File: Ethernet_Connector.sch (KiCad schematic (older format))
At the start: 1 part, among them Con2 WE-RJ45_7498011122AR

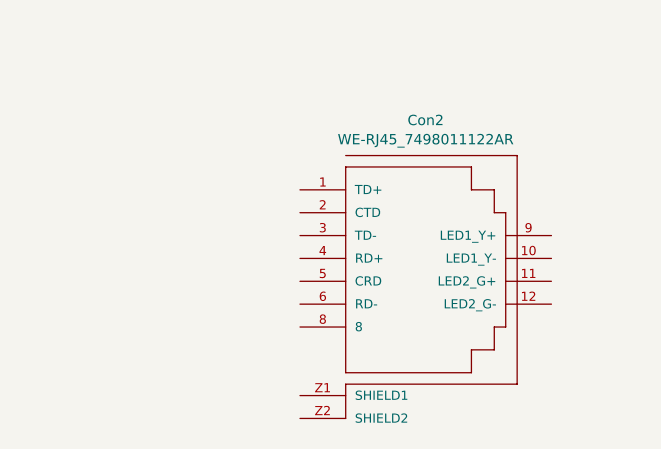
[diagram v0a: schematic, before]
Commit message: Added ethernet connector on pcb
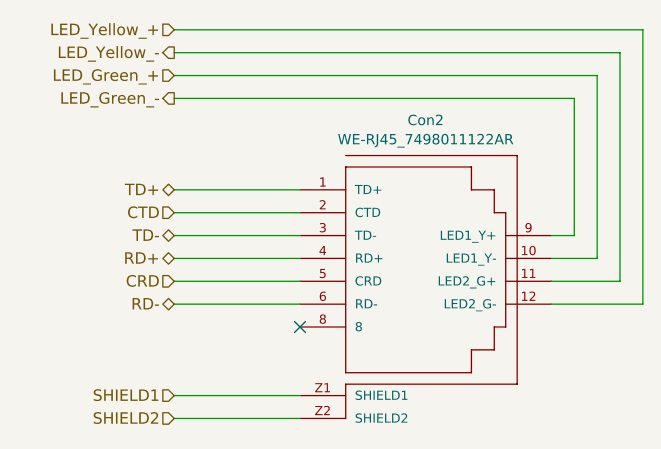
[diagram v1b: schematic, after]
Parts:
- Con2: footprint 7498011122AR_Eagle_WE-RJ45_rev20a_7498011122AR -> RJ45_Ethernet_Transformer:WE-RJ45_7498011122AR
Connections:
- net TD+: now reaches Con2.1 (TD+)
- net LED_Green_+: now reaches Con2.10 (LED1_Y-)
- net LED_Yellow_-: now reaches Con2.11 (LED2_G+)
- net LED_Yellow_+: now reaches Con2.12 (LED2_G-)
- net CTD: now reaches Con2.2 (CTD)
- net TD-: now reaches Con2.3 (TD-)
- net RD+: now reaches Con2.4 (RD+)
- net CRD: now reaches Con2.5 (CRD)
- net RD-: now reaches Con2.6 (RD-)
- net LED_Green_-: now reaches Con2.9 (LED1_Y+)
- net SHIELD1: now reaches Con2.Z1 (SHIELD1)
- net SHIELD2: now reaches Con2.Z2 (SHIELD2)
- no-connect marks 0 -> 1
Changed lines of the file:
@@
 F 0 "Con2" H 8000 6354 45  0000 C CNN
 F 1 "WE-RJ45_7498011122AR" H 8000 6270 45  0000 C CNN
-F 2 "7498011122AR_Eagle_WE-RJ45_rev20a_7498011122AR" H 7980 5800 20  0001 C CNN
+F 2 "RJ45_Ethernet_Transformer:WE-RJ45_7498011122AR" H 7980 5800 20  0001 C CNN
 F 3 "" H 7950 5650 50  0001 C CNN
 	1    7950 5650
 	1    0    0    -1
 $EndComp
+Wire Wire Line
+	7450 5250 6900 5250
+Wire Wire Line
+	7450 5350 6900 5350
+Wire Wire Line
+	7450 5450 6900 5450
+Wire Wire Line
+	7450 5550 6900 5550
+Wire Wire Line
+	7450 5650 6900 5650
+Wire Wire Line
+	7450 5750 6900 5750
+Wire Wire Line
+	8550 5450 8650 5450
+Wire Wire Line
+	8650 5450 8650 4850
+Wire Wire Line
+	8650 4850 6900 4850
+Wire Wire Line
+	8550 5550 8750 5550
+Wire Wire Line
+	8750 5550 8750 4750
+Wire Wire Line
+	8750 4750 6900 4750
+Wire Wire Line
+	8550 5650 8850 5650
+Wire Wire Line
+	8850 5650 8850 4650
+Wire Wire Line
+	8850 4650 6900 4650
+Wire Wire Line
+	8550 5750 8950 5750
+Wire Wire Line
+	8950 5750 8950 4550
+Wire Wire Line
+	8950 4550 6900 4550
+Wire Wire Line
+	7450 6150 6900 6150
+Wire Wire Line
+	7450 6250 6900 6250
+Text HLabel 6900 5250 0    50   BiDi ~ 0
+TD+
+Text HLabel 6900 5450 0    50   BiDi ~ 0
+TD-
+Text HLabel 6900 5550 0    50   BiDi ~ 0
+RD+
+Text HLabel 6900 5750 0    50   BiDi ~ 0
+RD-
+NoConn ~ 7450 5850
+Text HLabel 6900 6150 0    50   Input ~ 0
+SHIELD1
+Text HLabel 6900 6250 0    50   Input ~ 0
+SHIELD2
+Text HLabel 6900 5350 0    50   Input ~ 0
+CTD
+Text HLabel 6900 5650 0    50   Input ~ 0
+CRD
+Text HLabel 6900 4550 0    50   Input ~ 0
+LED_Yellow_+
+Text HLabel 6900 4650 0    50   Output ~ 0
+LED_Yellow_-
+Text HLabel 6900 4750 0    50   Input ~ 0
+LED_Green_+
+Text HLabel 6900 4850 0    50   Output ~ 0
+LED_Green_-
 $EndSCHEMATC

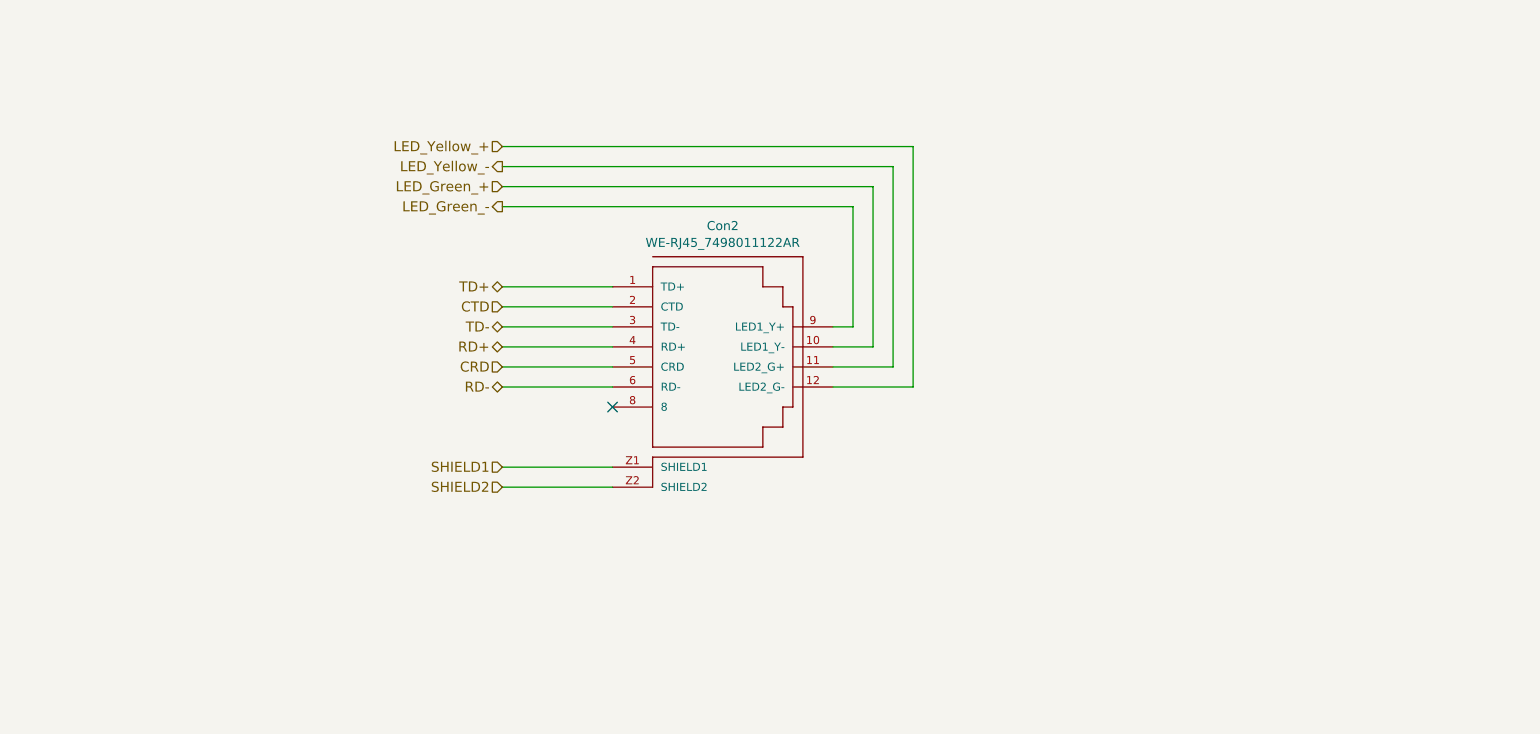
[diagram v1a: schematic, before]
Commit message: Added connection for ethernet modules
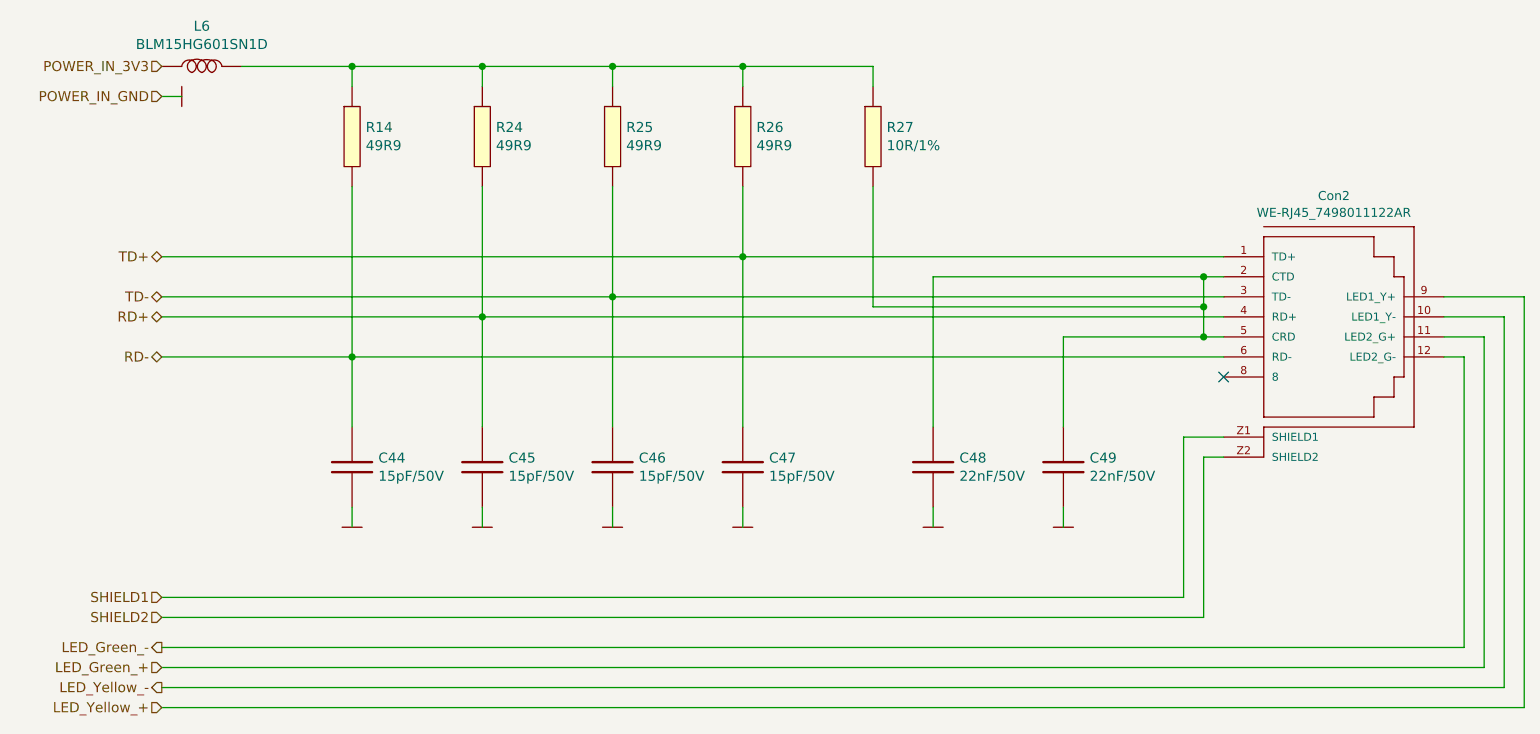
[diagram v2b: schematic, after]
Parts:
- added C44, C45, C46, C47: 15pF/50V, Capacitors_Smd_0603:15pF_0603, symbol Capacitors_Smd0603:15pF_0603
- added C48, C49: 22nF/50V, Capacitors_Smd_0603:22nF_0603, symbol Capacitors_Smd0603:22nF_0603
- added L6: BLM15HG601SN1D, Inductors:BLM15HG601SN1D_0402, symbol Inductors:BLM15HG601SN1D
- added R14, R24, R25, R26: 49R9, Resistor_Smd_0603:49R9_0603, symbol Resistors_Smd0603:49R9_0603
- added R27: 10R/1%, Resistor_Smd_0603:10R_0603, symbol Resistors_Smd0603:10R_0603_1%
- Con2: Developer (none) -> MW; Manufacturer (none) -> Wurth; Manufacturer Part Number (none) -> 7498011122AR; Package (none) -> SMD/SMT; Price@1000pcs (none) -> 27,98; Price@1pc (none) -> 40; Supplier (none) -> Mouser; Supplier Part Number (none) -> 710-7498011122AR; URL (none) -> https://pl.mouser.com/ProductDetail/Wurth-Elektronik/749801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
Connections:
- net CTD is gone; now on an unnamed net: Con2.2 (CTD)
- net LED_Green_+: now also Con2.11 (LED2_G+); no longer Con2.10 (LED1_Y-)
- net LED_Green_-: now also Con2.12 (LED2_G-); no longer Con2.9 (LED1_Y+)
- net LED_Yellow_+: now also Con2.9 (LED1_Y+); no longer Con2.12 (LED2_G-)
- net LED_Yellow_-: now also Con2.10 (LED1_Y-); no longer Con2.11 (LED2_G+)
- net RD+: now also C45.1, R24.2
- net RD-: now also C44.1, R14.2
- net TD+: now also C47.1, R26.2
- net TD-: now also C46.1, R25.2
- net CRD: no longer names the net of Con2.5 (CRD)
- net CRD: now also C48.1, C49.2, R27.2
- new net: L6.2, R14.1, R24.1, R25.1, R26.1, R27.1
- new net GND: C44.2, C45.2, C46.2, C47.2, C48.2, C49.1
- new net POWER_IN_3V3: L6.1

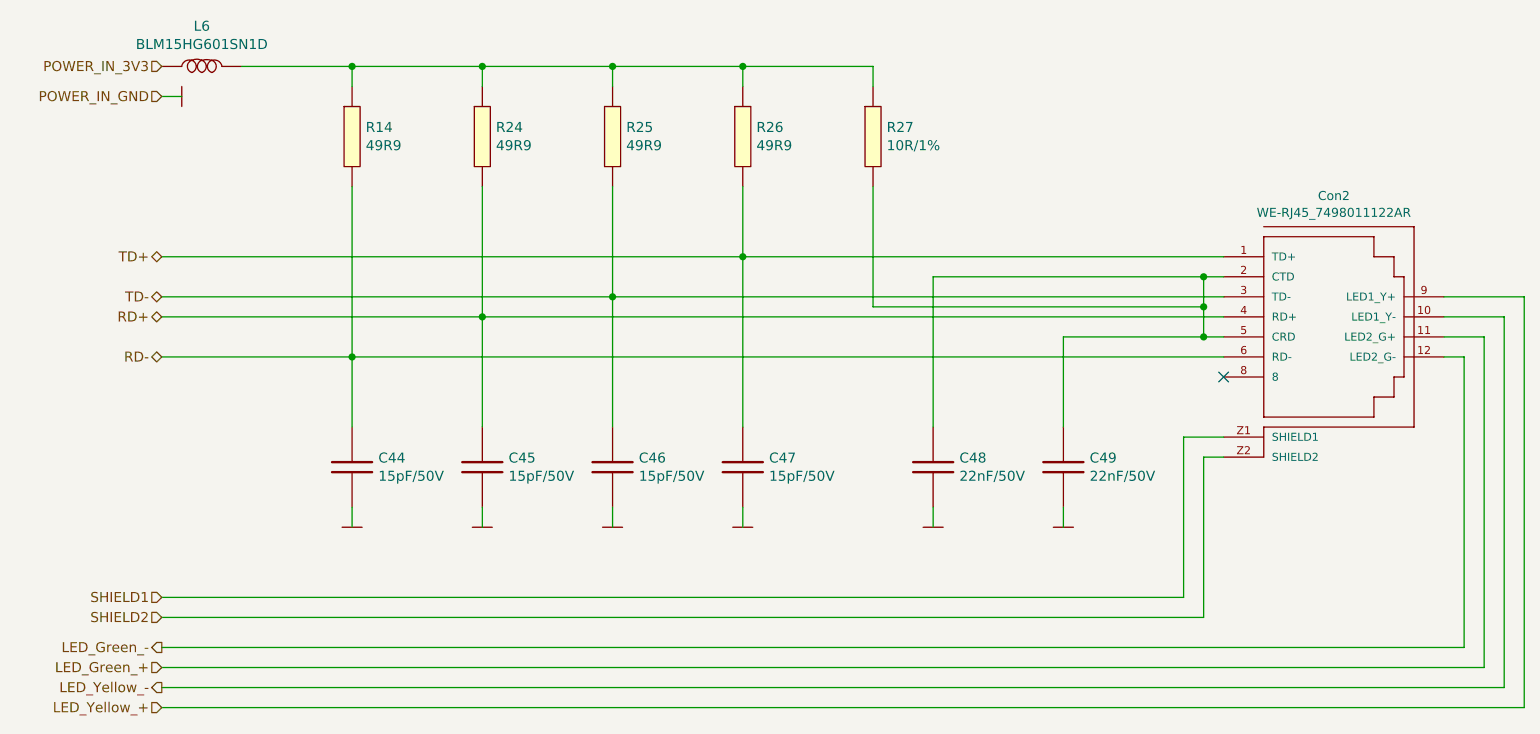
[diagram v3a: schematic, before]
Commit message: Updated README.md and figurated components on pcb
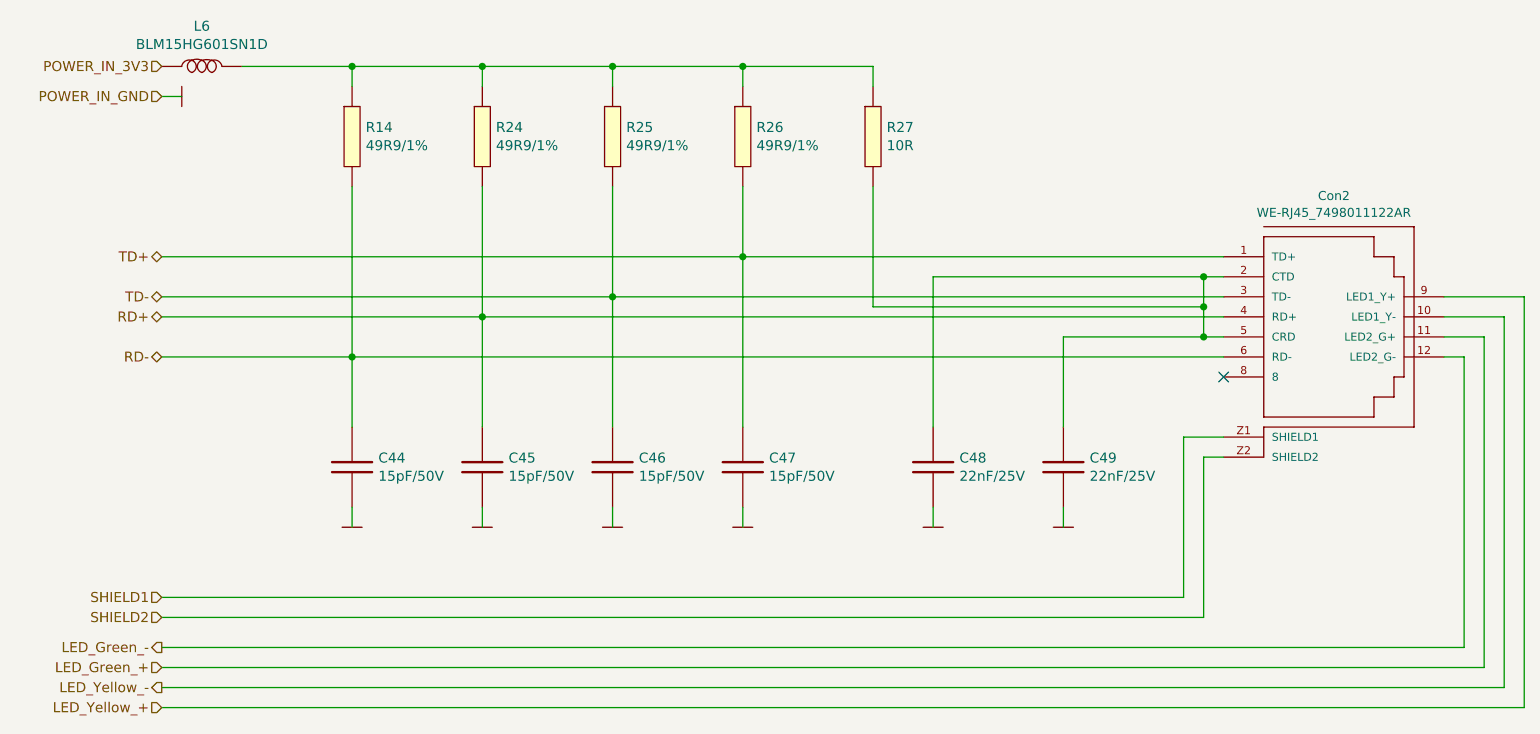
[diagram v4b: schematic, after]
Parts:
- removed C44, C45, C46, C47: 15pF/50V, Capacitors_Smd_0603:15pF_0603, symbol Capacitors_Smd0603:15pF_0603
- removed C48, C49: 22nF/50V, Capacitors_Smd_0603:22nF_0603, symbol Capacitors_Smd0603:22nF_0603
- removed R14, R24, R25, R26: 49R9, Resistor_Smd_0603:49R9_0603, symbol Resistors_Smd0603:49R9_0603
- removed R27: 10R/1%, Resistor_Smd_0603:10R_0603, symbol Resistors_Smd0603:10R_0603_1%
- added C44, C45, C46, C47: 15pF/50V, Capacitors_Smd_0402:15pF_0402, symbol Capacitors_Smd0402:15pF_0402
- added C48, C49: 22nF/25V, Capacitors_Smd_0402:22nF_0402, symbol Capacitors_Smd0402:22nF_0402
- added R14, R24, R25, R26: 49R9/1%, Resistor_Smd_0402:49R9_0402, symbol Resistors_Smd0402:49R9_0402_1%
- added R27: 10R, Resistor_Smd_0402:10R_0402, symbol Resistors_Smd0402:10R_0402
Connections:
- net GND: now also C44.2, C45.2, C46.2, C47.2, C48.2, C49.2
- net RD+: now also C45.1, R24.2
- net RD-: now also C44.1, R14.2
- net TD+: now also C47.1, R26.2
- net TD-: now also C46.1, R25.2
- net at Con2.2 (CTD), Con2.5 (CRD): now also C48.1, C49.1, R27.2
- net at L6.2: now also R14.1, R24.1, R25.1, R26.1, R27.1
